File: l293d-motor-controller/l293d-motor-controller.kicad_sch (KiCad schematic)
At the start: 13 parts, among them M1 Motor_DC, M2 Motor_DC, U1 LM7805, U2 L293D, U3 74HC04

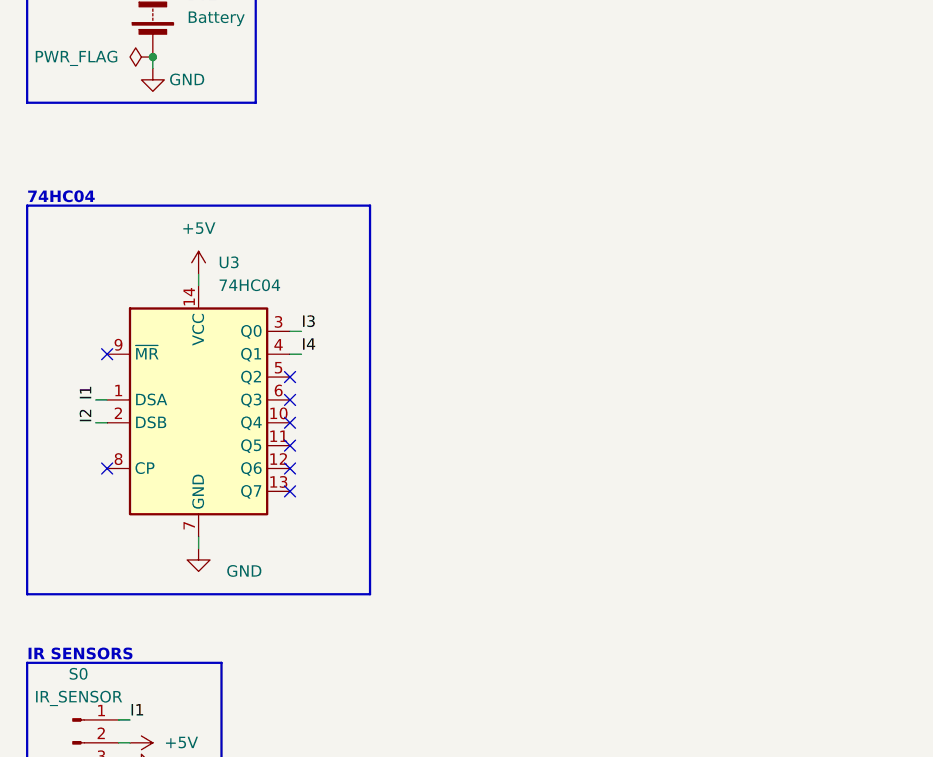
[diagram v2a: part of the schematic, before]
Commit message: project 3 / l293d motor driver / 74hc04 changed to cd4069
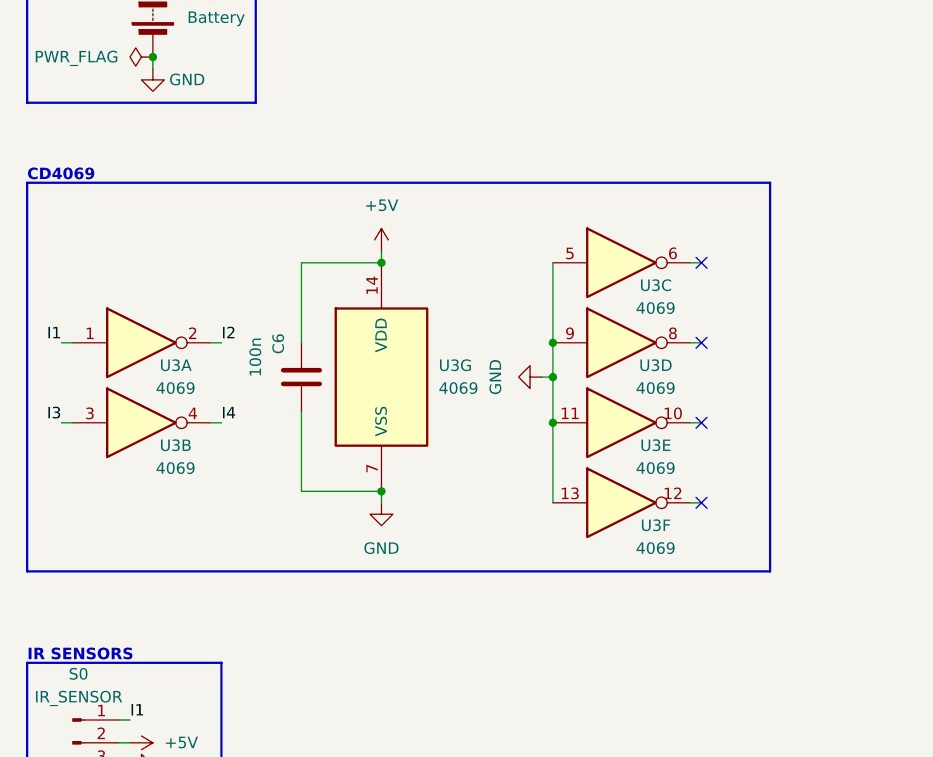
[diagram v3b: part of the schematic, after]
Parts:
- removed U3: 74HC04, Package_DIP:DIP-14_W7.62mm, symbol 74xx:74HC164
- added C6: 100n, Capacitor_THT:C_Disc_D3.0mm_W1.6mm_P2.50mm, symbol Device:C
- added U3: 4069, Package_DIP:DIP-14_W7.62mm, symbol 4xxx:4069
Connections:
- net +5V: now also C6.1, U3.14 (VDD)
- net GND: now also C6.2, U3.11, U3.13, U3.5, U3.7 (VSS), U3.9
- net I1: now also U3.1
- net I2: now also U3.2
- net I3: now also U3.3
- net I4: now also U3.4
- no-connect marks 10 -> 6
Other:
- note added: "CD4069"
- note removed: "74HC04"
